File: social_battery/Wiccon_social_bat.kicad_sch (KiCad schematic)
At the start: 20 parts, among them J1 SAO, SW1 Change, U1 CH32V003

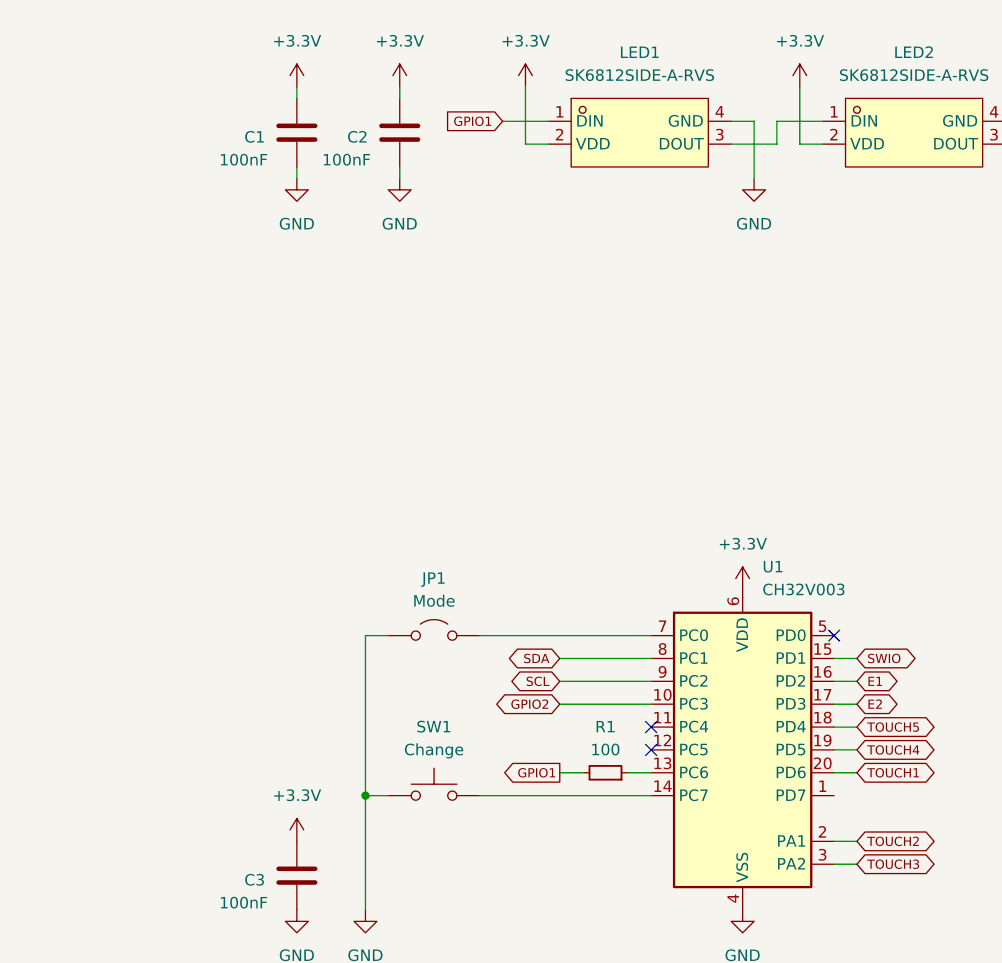
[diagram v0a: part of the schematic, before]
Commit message: Separate SAO IO1 from LED control on social battery, add firmware
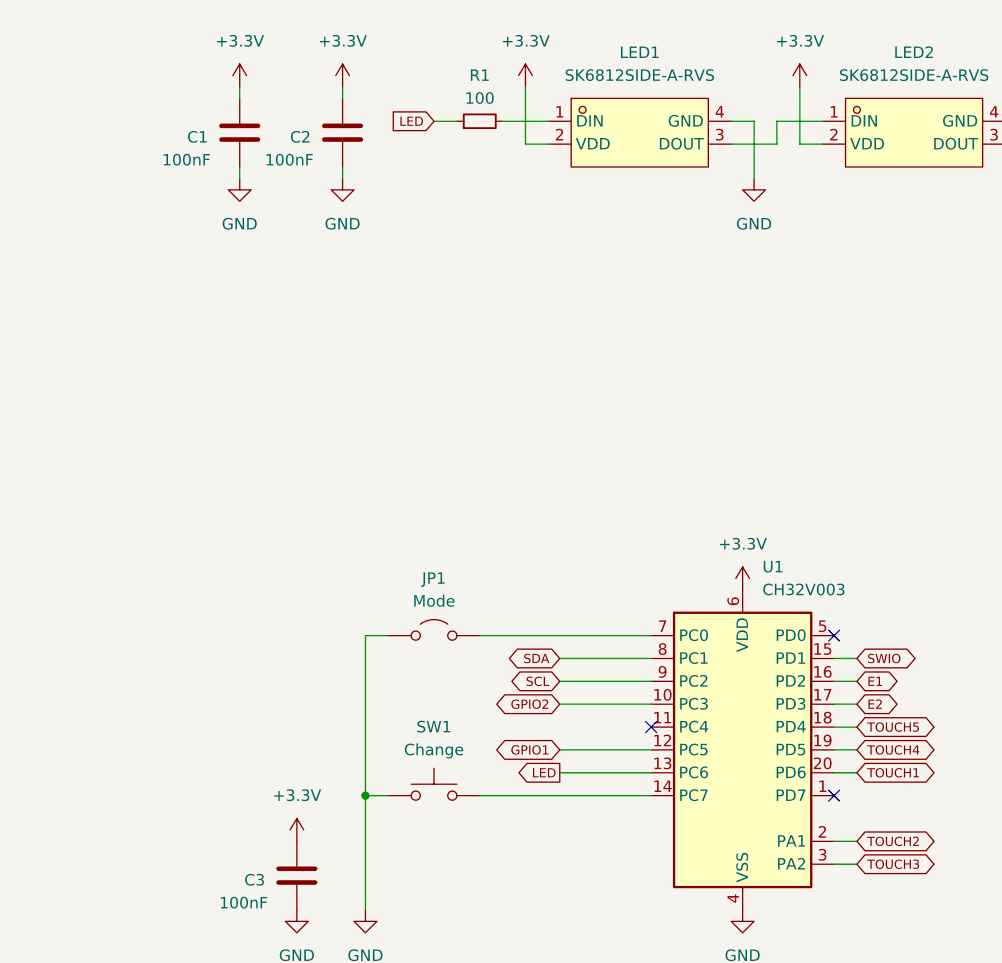
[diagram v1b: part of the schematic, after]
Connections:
- net GPIO1: now also U1.12 (PC5); no longer LED1.1 (DIN), R1.2
- net LED: now reaches R1.1, U1.13 (PC6)
- new net: LED1.1 (DIN), R1.2
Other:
- moved on the sheet: C1, C2
